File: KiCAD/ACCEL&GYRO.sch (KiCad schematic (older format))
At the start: 7 parts, among them J31 Conn_01x04, J32 Conn_01x03, J33 Conn_01x03, J34 Conn_01x04, U11 LSM6DS3

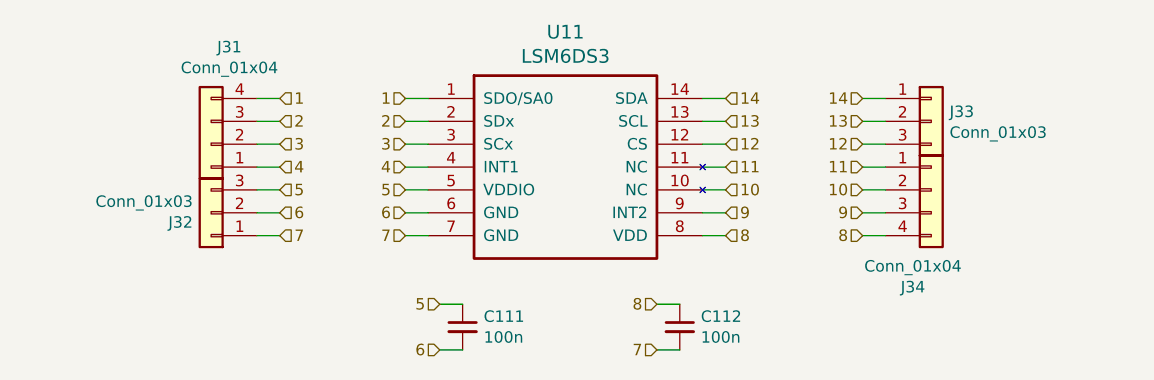
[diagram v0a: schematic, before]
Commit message: added usb, crystals
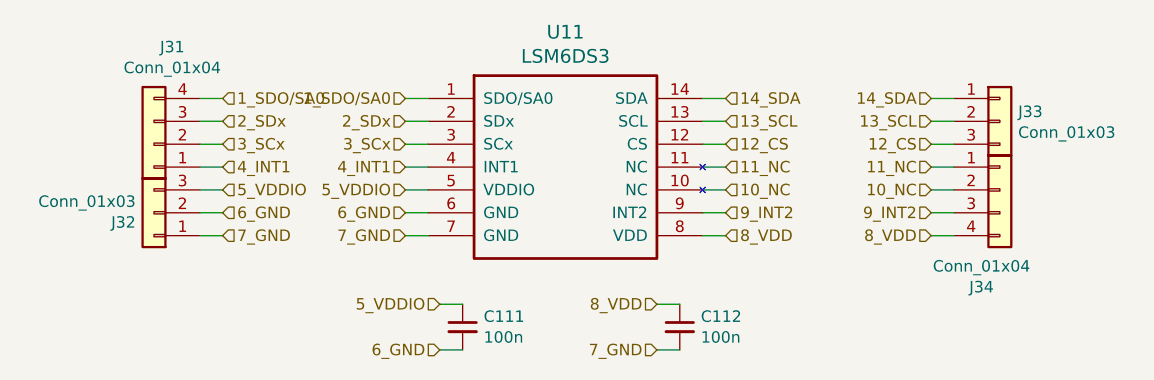
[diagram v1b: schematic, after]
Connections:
- net 1 renamed 1_SDO/SA0
- net 10 renamed 10_NC
- net 11 renamed 11_NC
- net 12 renamed 12_CS
- net 13 renamed 13_SCL
- net 14 renamed 14_SDA
- net 2 renamed 2_SDx
- net 3 renamed 3_SCx
- net 4 renamed 4_INT1
- net 5 renamed 5_VDDIO
- net 6 renamed 6_GND
- net 7 renamed 7_GND
- net 8 renamed 8_VDD
- net 9 renamed 9_INT2
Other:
- moved on the sheet: J31, J32, J33, J34
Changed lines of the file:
@@
 $Descr A4 11693 8268
 encoding utf-8
-Sheet 12 17
+Sheet 12 18
 Title ""
 Date ""
@@
 $EndComp
 Text HLabel 3700 5800 0    50   Input ~ 0
-1
+1_SDO/SA0
 Wire Wire Line
 	3700 5800 3800 5800
 Text HLabel 3700 5900 0    50   Input ~ 0
-2
+2_SDx
 Wire Wire Line
 	3700 5900 3800 5900
 Text HLabel 3700 6000 0    50   Input ~ 0
-3
+3_SCx
 Wire Wire Line
 	3700 6000 3800 6000
 Text HLabel 3700 6100 0    50   Input ~ 0
-4
+4_INT1
 Wire Wire Line
 	3700 6100 3800 6100
 Text HLabel 3700 6200 0    50   Input ~ 0
-5
+5_VDDIO
 Wire Wire Line
 	3700 6200 3800 6200
 Text HLabel 3700 6300 0    50   Input ~ 0
-6
+6_GND
 Wire Wire Line
 	3700 6300 3800 6300
 Text HLabel 3700 6400 0    50   Input ~ 0
-7
+7_GND
 Wire Wire Line
 	3700 6400 3800 6400
 Text HLabel 5100 5800 2    50   Input ~ 0
-14
+14_SDA
 Wire Wire Line
 	5100 5800 5000 5800
 Text HLabel 5100 5900 2    50   Input ~ 0
-13
+13_SCL
 Wire Wire Line
 	5100 5900 5000 5900
 Text HLabel 5100 6000 2    50   Input ~ 0
-12
+12_CS
 Wire Wire Line
 	5100 6000 5000 6000
 Text HLabel 5100 6100 2    50   Input ~ 0
-11
+11_NC
 Wire Wire Line
 	5100 6100 5000 6100
 Text HLabel 5100 6200 2    50   Input ~ 0
-10
+10_NC
 Wire Wire Line
 	5100 6200 5000 6200
 Text HLabel 5100 6300 2    50   Input ~ 0
-9
+9_INT2
 Wire Wire Line
 	5100 6300 5000 6300
 Text HLabel 5100 6400 2    50   Input ~ 0
-8
+8_VDD
 Wire Wire Line
 	5100 6400 5000 6400
@@
 L Connector_Generic:Conn_01x03 J?
 U 1 1 5CDC27EB
-P 2850 6300
+P 2600 6300
 AR Path="/5CDC27EB" Ref="J?"  Part="1"
 AR Path="/5CDAC31F/5CDC27EB" Ref="J?"  Part="1"
@@
 AR Path="/5D23D721/5CDC27EB" Ref="J?"  Part="1"
 AR Path="/5CDC1D3D/5CDC27EB" Ref="J32"  Part="1"
-F 0 "J32" H 2930 6342 50  0000 L CNN
-F 1 "Conn_01x03" H 2930 6251 50  0000 L CNN
-F 2 "Connector_PinHeader_2.54mm:PinHeader_1x03_P2.54mm_Vertical" H 2850 6300 50  0001 C CNN
-F 3 "~" H 2850 6300 50  0001 C CNN
-	1    2850 6300
+F 0 "J32" H 2680 6342 50  0000 L CNN
+F 1 "Conn_01x03" H 2680 6251 50  0000 L CNN
+F 2 "Connector_PinHeader_2.54mm:PinHeader_1x03_P2.54mm_Vertical" H 2600 6300 50  0001 C CNN
+F 3 "~" H 2600 6300 50  0001 C CNN
+	1    2600 6300
 	-1   0    0    1
 $EndComp
@@
 L Connector_Generic:Conn_01x04 J?
 U 1 1 5CDC2CFF
-P 2850 6000
+P 2600 6000
 AR Path="/5CDC2CFF" Ref="J?"  Part="1"
 AR Path="/5CDACD1E/5CDC2CFF" Ref="J?"  Part="1"
 AR Path="/5CDC1D3D/5CDC2CFF" Ref="J31"  Part="1"
-F 0 "J31" H 2770 5575 50  0000 C CNN
-F 1 "Conn_01x04" H 2770 5666 50  0000 C CNN
-F 2 "Connector_PinHeader_2.54mm:PinHeader_1x04_P2.54mm_Vertical" H 2850 6000 50  0001 C CNN
-F 3 "~" H 2850 6000 50  0001 C CNN
-	1    2850 6000
+F 0 "J31" H 2520 5575 50  0000 C CNN
+F 1 "Conn_01x04" H 2520 5666 50  0000 C CNN
+F 2 "Connector_PinHeader_2.54mm:PinHeader_1x04_P2.54mm_Vertical" H 2600 6000 50  0001 C CNN
+F 3 "~" H 2600 6000 50  0001 C CNN
+	1    2600 6000
 	-1   0    0    1
 $EndComp
-Text HLabel 3150 6200 2    50   Input ~ 0
-5
-Wire Wire Line
-	3150 6200 3050 6200
-Text HLabel 3150 6400 2    50   Input ~ 0
-7
-Wire Wire Line
-	3150 6400 3050 6400
+Text HLabel 2900 6200 2    50   Input ~ 0
+5_VDDIO
+Wire Wire Line
+	2900 6200 2800 6200
+Text HLabel 2900 6400 2    50   Input ~ 0
+7_GND
+Wire Wire Line
+	2900 6400 2800 6400
 $Comp
 L Device:C_Small C?
@@
 	1    0    0    -1
 $EndComp
-Text HLabel 3150 5800 2    50   Input ~ 0
-1
-Wire Wire Line
-	3150 5800 3050 5800
-Text HLabel 3150 6300 2    50   Input ~ 0
-6
-Wire Wire Line
-	3150 6300 3050 6300
+Text HLabel 2900 5800 2    50   Input ~ 0
+1_SDO/SA0
+Wire Wire Line
+	2900 5800 2800 5800
+Text HLabel 2900 6300 2    50   Input ~ 0
+6_GND
+Wire Wire Line
+	2900 6300 2800 6300
 $Comp
 L Device:C_Small C?
@@
 	1    0    0    -1
 $EndComp
-Text HLabel 3150 5900 2    50   Input ~ 0
-2
-Wire Wire Line
-	3150 5900 3050 5900
-Text HLabel 3150 6100 2    50   Input ~ 0
-4
-Wire Wire Line
-	3150 6100 3050 6100
-Text HLabel 3150 6000 2    50   Input ~ 0
-3
-Wire Wire Line
-	3150 6000 3050 6000
+Text HLabel 2900 5900 2    50   Input ~ 0
+2_SDx
+Wire Wire Line
+	2900 5900 2800 5900
+Text HLabel 2900 6100 2    50   Input ~ 0
+4_INT1
+Wire Wire Line
+	2900 6100 2800 6100
+Text HLabel 2900 6000 2    50   Input ~ 0
+3_SCx
+Wire Wire Line
+	2900 6000 2800 6000
 $Comp
 L Connector_Generic:Conn_01x03 J?
 U 1 1 5CDC4A8B
-P 6000 5900
+P 6300 5900
 AR Path="/5CDC4A8B" Ref="J?"  Part="1"
 AR Path="/5CDAC31F/5CDC4A8B" Ref="J?"  Part="1"
@@
 AR Path="/5D23D721/5CDC4A8B" Ref="J?"  Part="1"
 AR Path="/5CDC1D3D/5CDC4A8B" Ref="J33"  Part="1"
-F 0 "J33" H 6080 5942 50  0000 L CNN
-F 1 "Conn_01x03" H 6080 5851 50  0000 L CNN
-F 2 "Connector_PinHeader_2.54mm:PinHeader_1x03_P2.54mm_Vertical" H 6000 5900 50  0001 C CNN
-F 3 "~" H 6000 5900 50  0001 C CNN
-	1    6000 5900
+F 0 "J33" H 6380 5942 50  0000 L CNN
+F 1 "Conn_01x03" H 6380 5851 50  0000 L CNN
+F 2 "Connector_PinHeader_2.54mm:PinHeader_1x03_P2.54mm_Vertical" H 6300 5900 50  0001 C CNN
+F 3 "~" H 6300 5900 50  0001 C CNN
+	1    6300 5900
 	1    0    0    -1
 $EndComp
@@
 L Connector_Generic:Conn_01x04 J?
 U 1 1 5CDC4A91
-P 6000 6200
+P 6300 6200
 AR Path="/5CDC4A91" Ref="J?"  Part="1"
 AR Path="/5CDACD1E/5CDC4A91" Ref="J?"  Part="1"
 AR Path="/5CDC1D3D/5CDC4A91" Ref="J34"  Part="1"
-F 0 "J34" H 5920 5775 50  0000 C CNN
-F 1 "Conn_01x04" H 5920 5866 50  0000 C CNN
-F 2 "Connector_PinHeader_2.54mm:PinHeader_1x04_P2.54mm_Vertical" H 6000 6200 50  0001 C CNN
-F 3 "~" H 6000 6200 50  0001 C CNN
-	1    6000 6200
-	1    0    0    -1
-$EndComp
-Wire Wire Line
-	5700 6000 5800 6000
-Wire Wire Line
-	5700 5800 5800 5800
-Wire Wire Line
-	5700 6400 5800 6400
-Wire Wire Line
-	5700 5900 5800 5900
-Wire Wire Line
-	5700 6300 5800 6300
-Wire Wire Line
-	5700 6100 5800 6100
-Wire Wire Line
-	5700 6200 5800 6200
-Text HLabel 5700 5800 0    50   Input ~ 0
-14
-Text HLabel 5700 5900 0    50   Input ~ 0
-13
-Text HLabel 5700 6000 0    50   Input ~ 0
-12
-Text HLabel 5700 6100 0    50   Input ~ 0
-11
-Text HLabel 5700 6200 0    50   Input ~ 0
-10
-Text HLabel 5700 6300 0    50   Input ~ 0
-9
-Text HLabel 5700 6400 0    50   Input ~ 0
-8
+F 0 "J34" H 6220 5775 50  0000 C CNN
+F 1 "Conn_01x04" H 6220 5866 50  0000 C CNN
+F 2 "Connector_PinHeader_2.54mm:PinHeader_1x04_P2.54mm_Vertical" H 6300 6200 50  0001 C CNN
+F 3 "~" H 6300 6200 50  0001 C CNN
+	1    6300 6200
+	1    0    0    -1
+$EndComp
+Wire Wire Line
+	6000 6000 6100 6000
+Wire Wire Line
+	6000 5800 6100 5800
+Wire Wire Line
+	6000 6400 6100 6400
+Wire Wire Line
+	6000 5900 6100 5900
+Wire Wire Line
+	6000 6300 6100 6300
+Wire Wire Line
+	6000 6100 6100 6100
+Wire Wire Line
+	6000 6200 6100 6200
+Text HLabel 6000 5800 0    50   Input ~ 0
+14_SDA
+Text HLabel 6000 5900 0    50   Input ~ 0
+13_SCL
+Text HLabel 6000 6000 0    50   Input ~ 0
+12_CS
+Text HLabel 6000 6100 0    50   Input ~ 0
+11_NC
+Text HLabel 6000 6200 0    50   Input ~ 0
+10_NC
+Text HLabel 6000 6300 0    50   Input ~ 0
+9_INT2
+Text HLabel 6000 6400 0    50   Input ~ 0
+8_VDD
 Text HLabel 3850 6700 0    50   Input ~ 0
-5
+5_VDDIO
 Wire Wire Line
 	3850 6700 3950 6700
 Text HLabel 3850 6900 0    50   Input ~ 0
-6
+6_GND
 Wire Wire Line
 	3850 6900 3950 6900
 Text HLabel 4800 6700 0    50   Input ~ 0
-8
+8_VDD
 Wire Wire Line
 	4800 6700 4900 6700
 Text HLabel 4800 6900 0    50   Input ~ 0
-7
+7_GND
 Wire Wire Line
 	4800 6900 4900 6900
